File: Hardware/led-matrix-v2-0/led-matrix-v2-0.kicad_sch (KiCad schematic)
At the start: 517 parts, among them J1 Conn_01x04_Socket, U1 SN74AHCT125DR

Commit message: routed power
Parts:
- removed PS1: OKR-T/10-W12-C, Various_LED_Board:CONV_OKR-T_10-W12-C, symbol OKR-T_10-W12-C:OKR-T/10-W12-C
- removed R1: 267, Resistor_SMD:R_0805_2012Metric, symbol Device:R
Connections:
- no-connect marks 9 -> 8

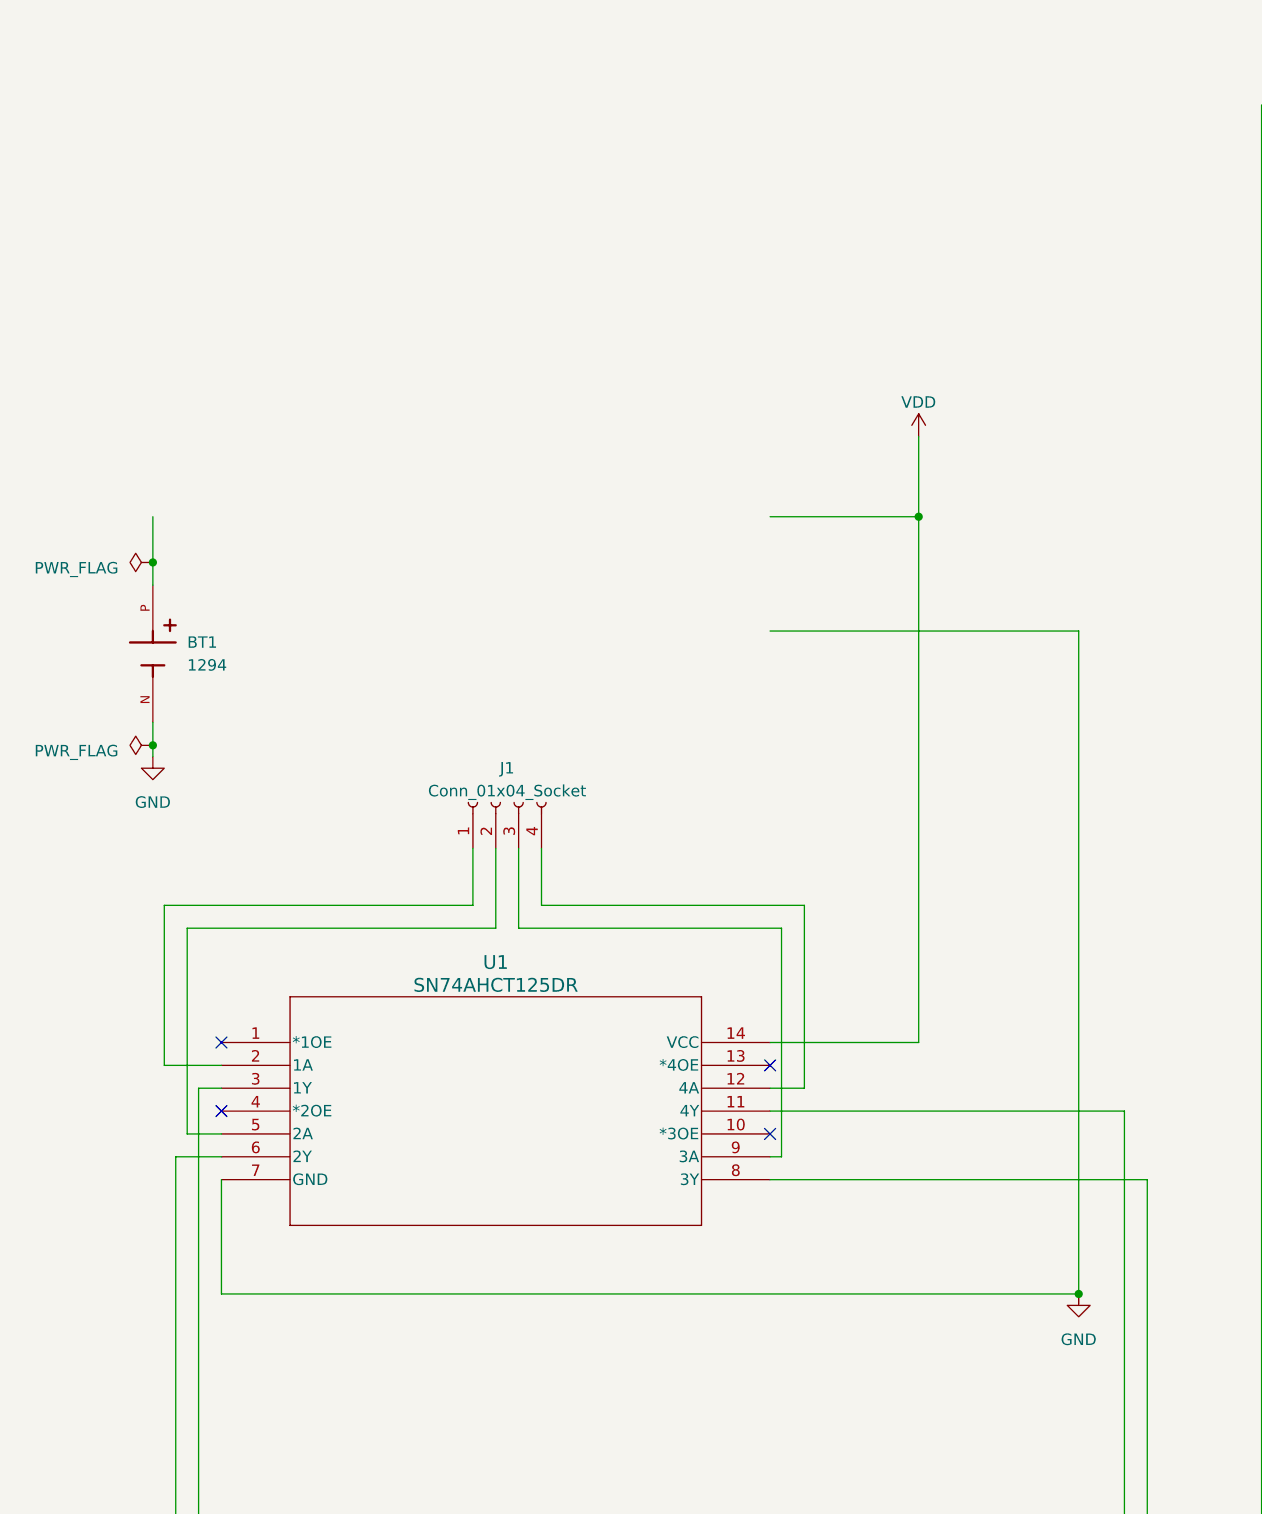
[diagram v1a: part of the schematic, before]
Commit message: switched to usb c from battery
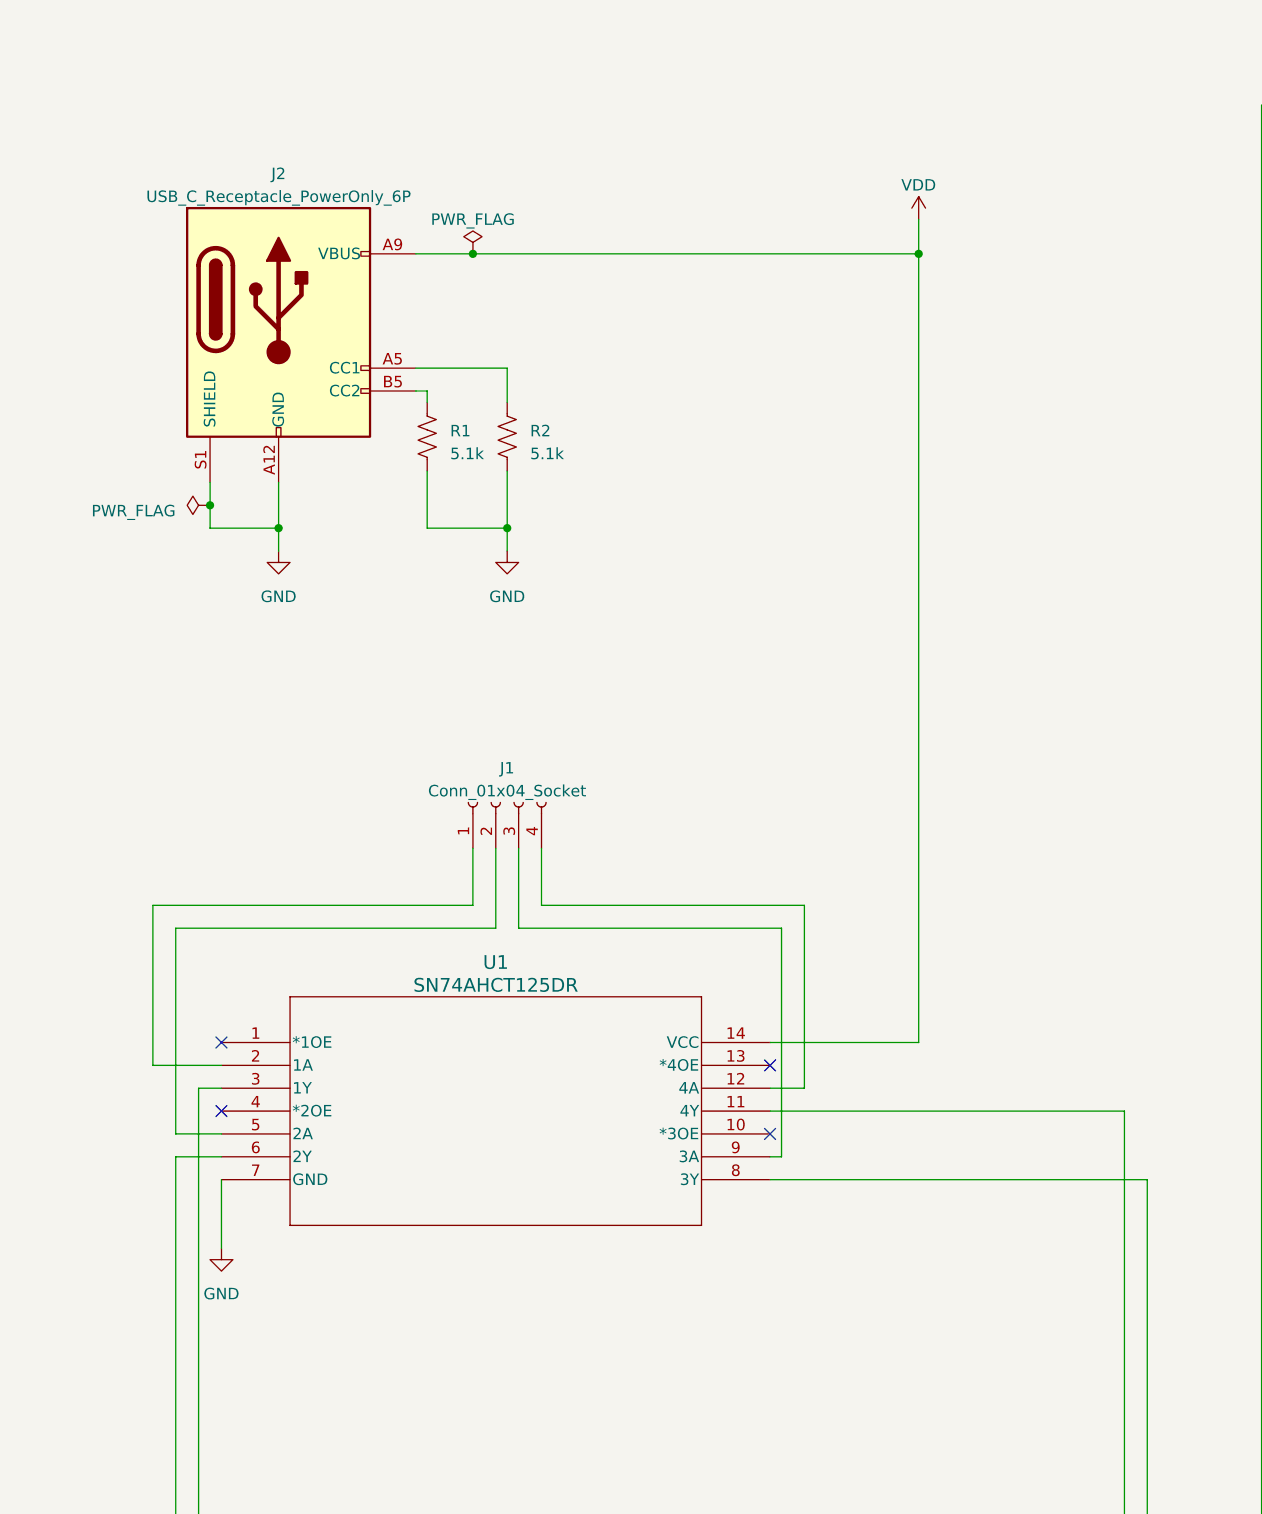
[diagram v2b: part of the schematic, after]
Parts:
- removed BT1: 1294, Various_LED_Board:BAT_1294, symbol 1294:1294
- added J2: USB_C_Receptacle_PowerOnly_6P, Various_LED_Board:USB_C_CUI_UJC-HP-3-SMT-TR, symbol Connector:USB_C_Receptacle_PowerOnly_6P
- added R1, R2: 5.1k, Resistor_SMD:R_0805_2012Metric, symbol Device:R_US
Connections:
- net GND: now also J2.A12 (GND), J2.B12 (GND), J2.S1 (SHIELD), R1.2, R2.2
- net VDD: now also J2.A9 (VBUS), J2.B9 (VBUS)
- new net: J2.B5 (CC2), R1.1
- new net: J2.A5 (CC1), R2.1
